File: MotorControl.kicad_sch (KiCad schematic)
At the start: 4 parts, among them U3 CSD18534Q5A, U4 CSD18534Q5A, U5 CSD18534Q5A

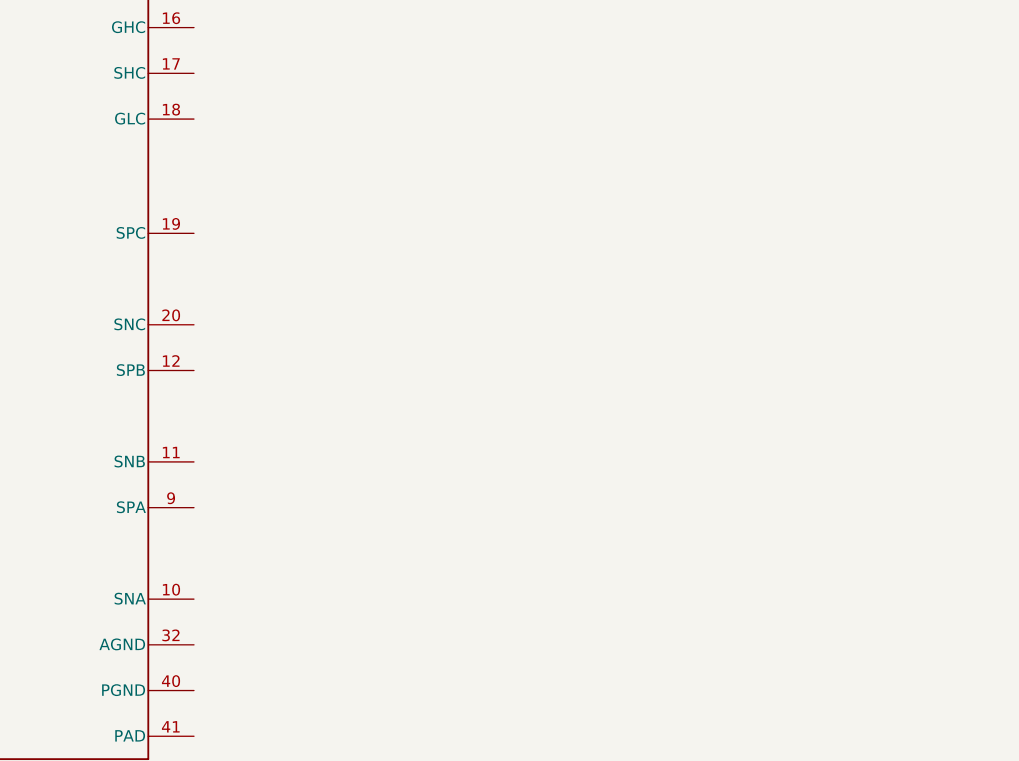
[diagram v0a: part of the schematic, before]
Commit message: wire sense resistors
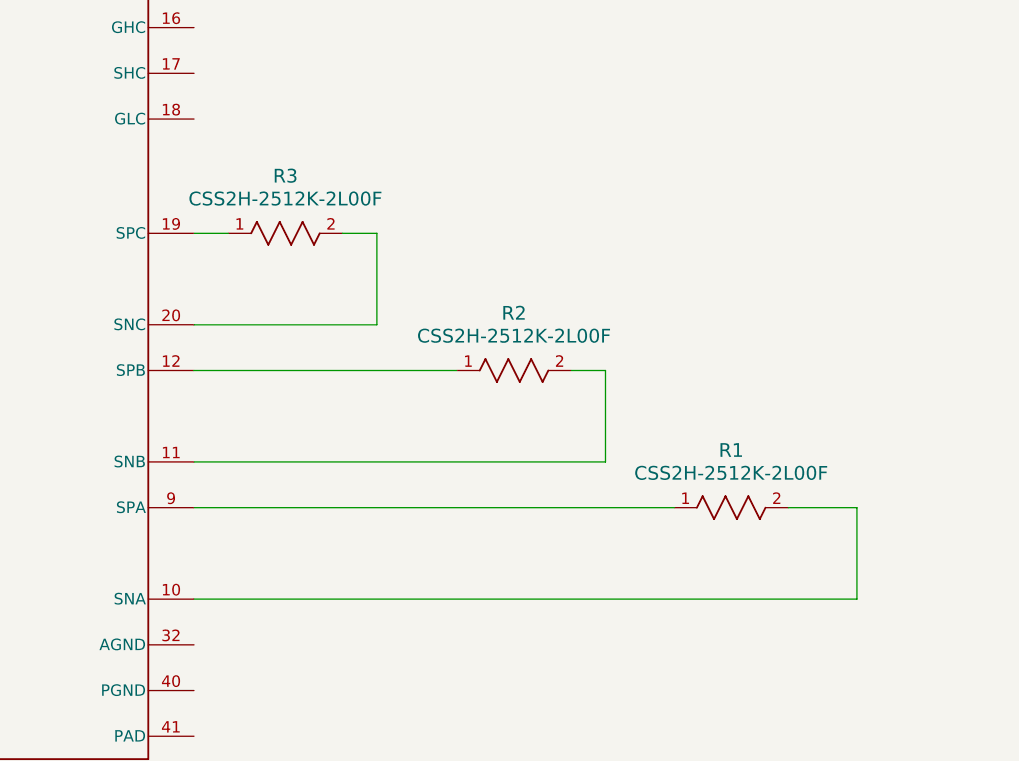
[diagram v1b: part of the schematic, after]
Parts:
- added R1, R2, R3: CSS2H-2512K-2L00F, RES_2L00x_BRN, symbol CSS2H_2512K_2L00F:CSS2H-2512K-2L00F
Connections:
- net at U?.10 (SNA): now also R1.2
- net at U?.11 (SNB): now also R2.2
- net at U?.12 (SPB): now also R2.1
- net at U?.19 (SPC): now also R3.1
- net at U?.20 (SNC): now also R3.2
- net at U?.9 (SPA): now also R1.1

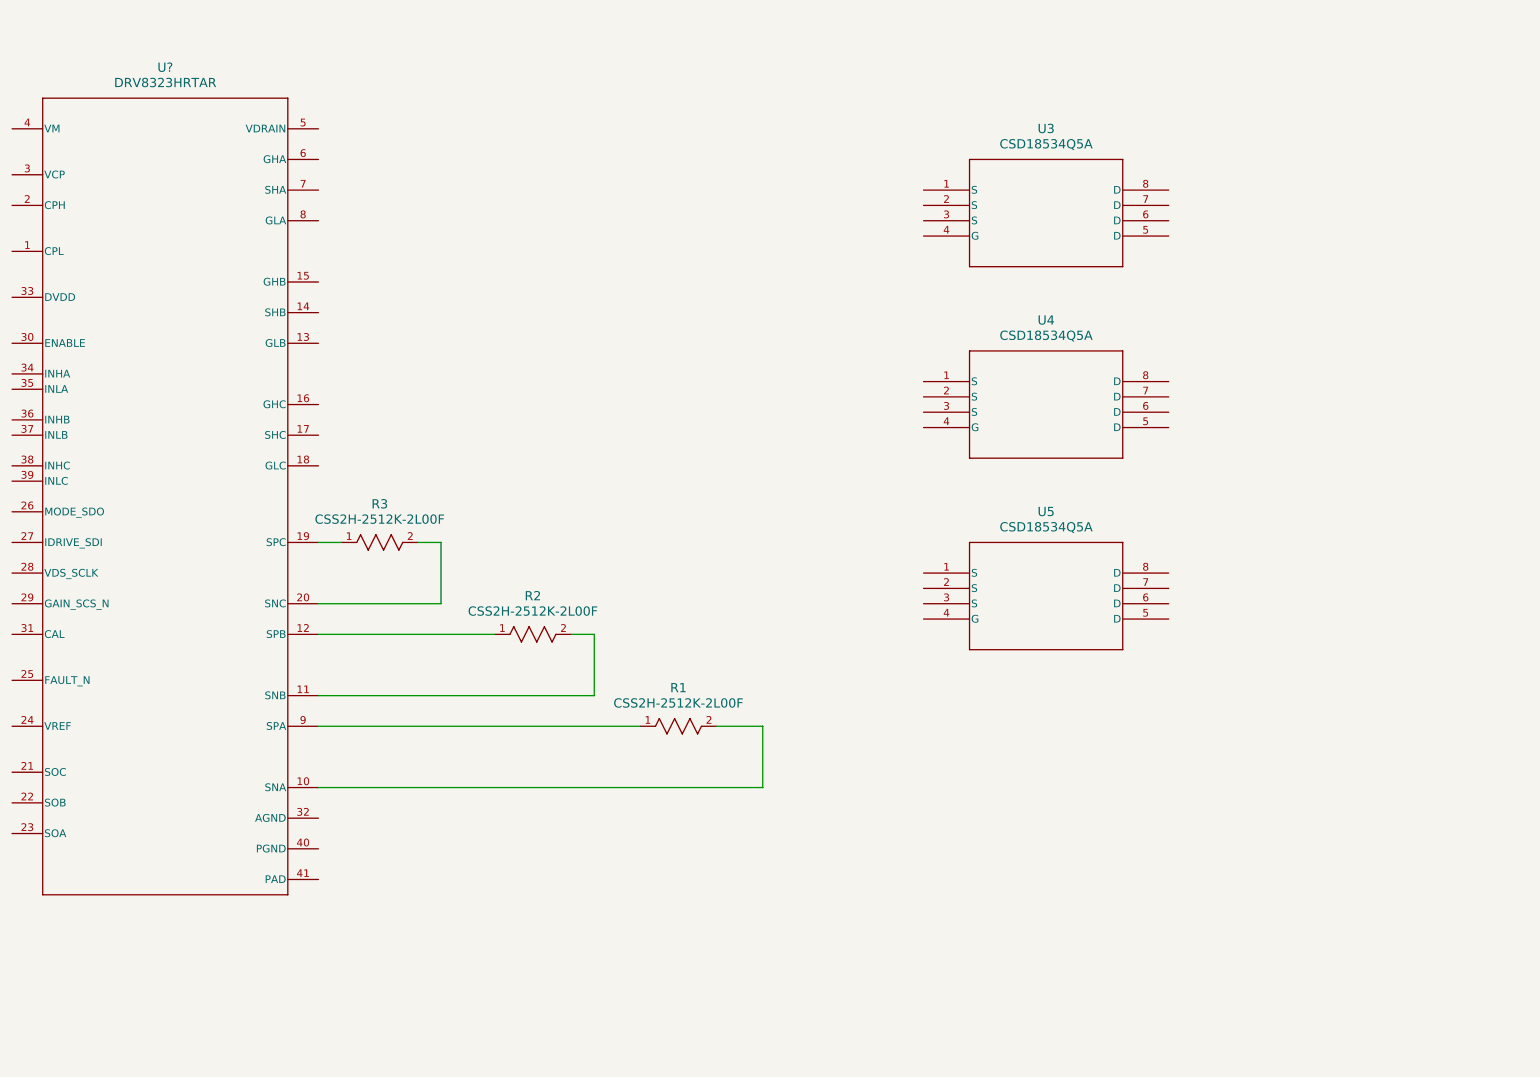
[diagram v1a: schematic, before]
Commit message: routed motor driver fets and shunts
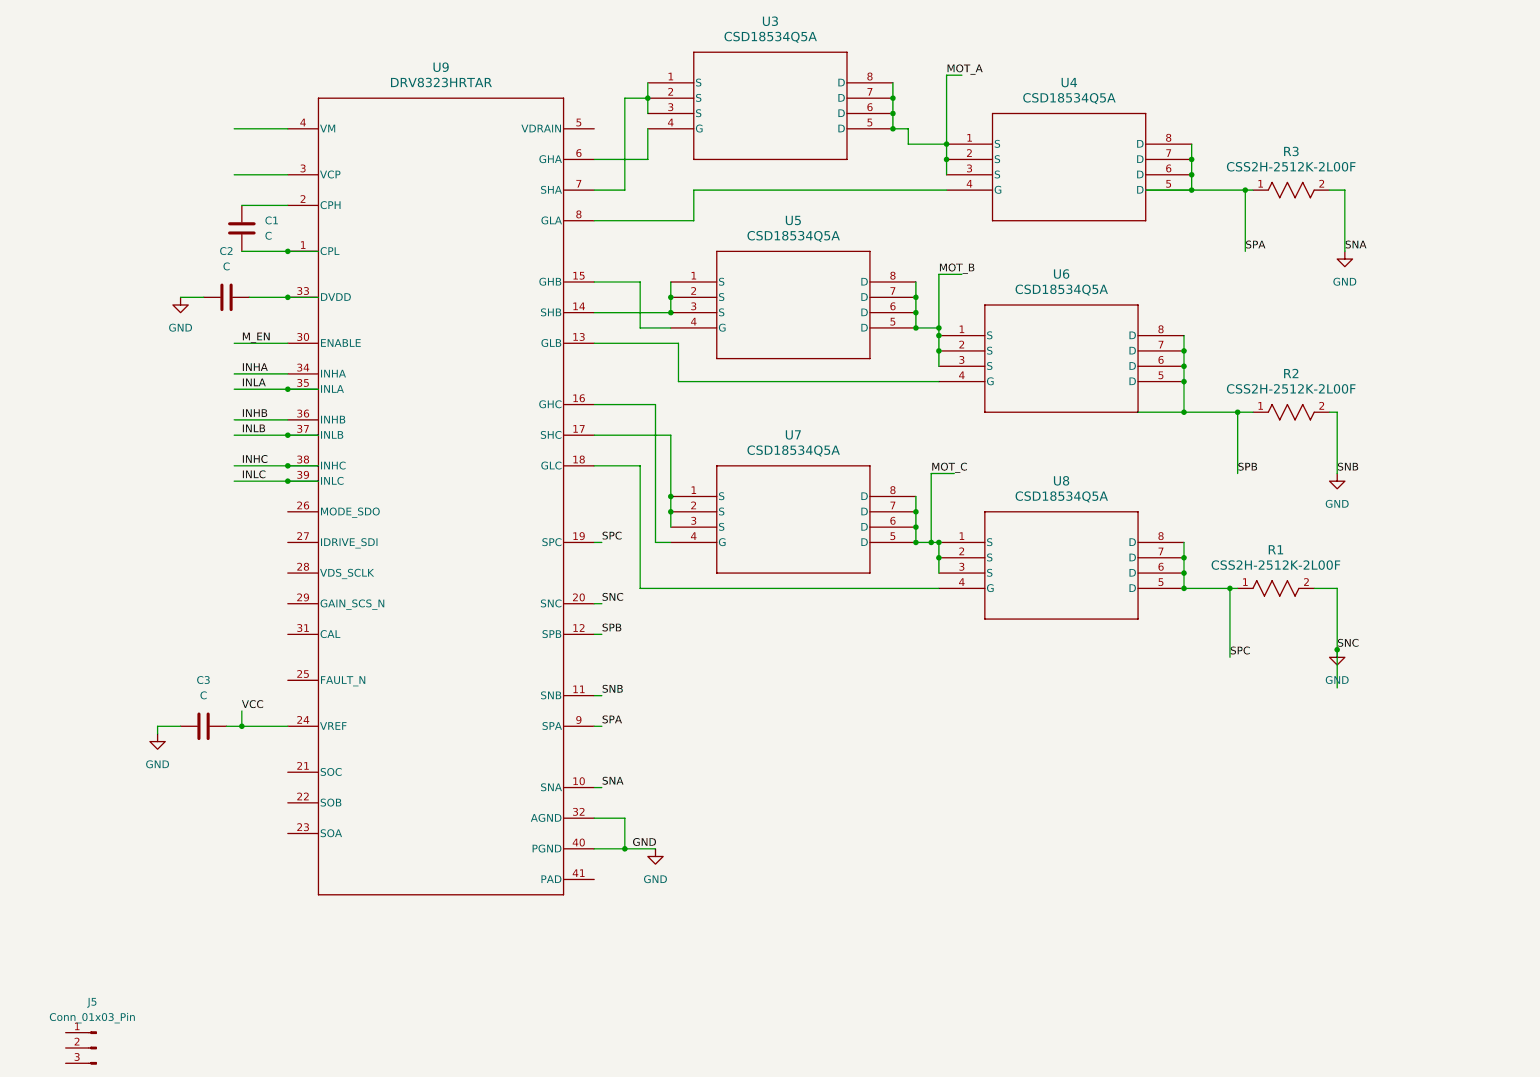
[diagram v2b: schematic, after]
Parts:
- added C1, C2, C3: C, symbol Device:C
- added J5: Conn_01x03_Pin, symbol Connector:Conn_01x03_Pin
- added U6, U7, U8: CSD18534Q5A, DQJ8, symbol CSD18534Q5A:CSD18534Q5A
- R1, R2, R3: footprint RES_2L00x_BRN -> Resistor_SMD:R_2512_6332Metric_Pad1.40x3.35mm_HandSolder
- gave numbers to parts that had none: 1
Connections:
- net SPA: now reaches U9.9 (SPA)
- net SPA: now also R3.1, U4.5 (D), U4.6 (D), U4.7 (D), U4.8 (D); no longer R1.1
- net GND: now reaches R1.2, U9.10 (SNA)
- net GND: now also R2.2, R3.2, U9.11 (SNB), U9.20 (SNC), U9.32 (AGND), U9.40 (PGND), C2.1, C3.1
- net at U5.1 (S): now also U5.2 (S), U5.3 (S), U9.14 (SHB)
- net at U5.4 (G): now also U9.15 (GHB)
- net MOT_B: now reaches U5.5 (D)
- net MOT_B: now also U5.6 (D), U5.7 (D), U5.8 (D), U6.1 (S), U6.2 (S), U6.3 (S)
- net at U9.1 (CPL): now also C1.2
- net SPB: now reaches R2.1, U9.12 (SPB)
- net SPB: now also U6.5 (D), U6.6 (D), U6.7 (D), U6.8 (D)
- net at U9.13 (GLB): now also U6.4 (G)
- net at U9.16 (GHC): now also U7.4 (G)
- net at U9.17 (SHC): now also U7.1 (S), U7.2 (S), U7.3 (S)
- net at U9.18 (GLC): now also U8.4 (G)
- net SPC: now reaches U9.19 (SPC)
- net SPC: now also R1.1, U8.5 (D), U8.6 (D), U8.7 (D), U8.8 (D); no longer R3.1
- net at U9.2 (CPH): now also C1.1
- net VCC: now reaches U9.24 (VREF)
- net VCC: now also C3.2
- net M_EN: now reaches U9.30 (ENABLE)
- net at U9.33 (DVDD): now also C2.2
- net INHA: now reaches U9.34 (INHA)
- net INLA: now reaches U9.35 (INLA)
- net INHB: now reaches U9.36 (INHB)
- net INLB: now reaches U9.37 (INLB)
- net INHC: now reaches U9.38 (INHC)
- net INLC: now reaches U9.39 (INLC)
- net at U9.6 (GHA): now also U3.4 (G)
- net at U9.7 (SHA): now also U3.1 (S), U3.2 (S), U3.3 (S)
- net at U9.8 (GLA): now also U4.4 (G)
- net MOT_A: now reaches U3.5 (D)
- net MOT_A: now also U3.6 (D), U3.7 (D), U3.8 (D), U4.1 (S), U4.2 (S), U4.3 (S)
- new net MOT_C: U7.5 (D), U7.6 (D), U7.7 (D), U7.8 (D), U8.1 (S), U8.2 (S), U8.3 (S)
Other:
- moved on the sheet: R1, R2, R3, U3, U4, U5, U9

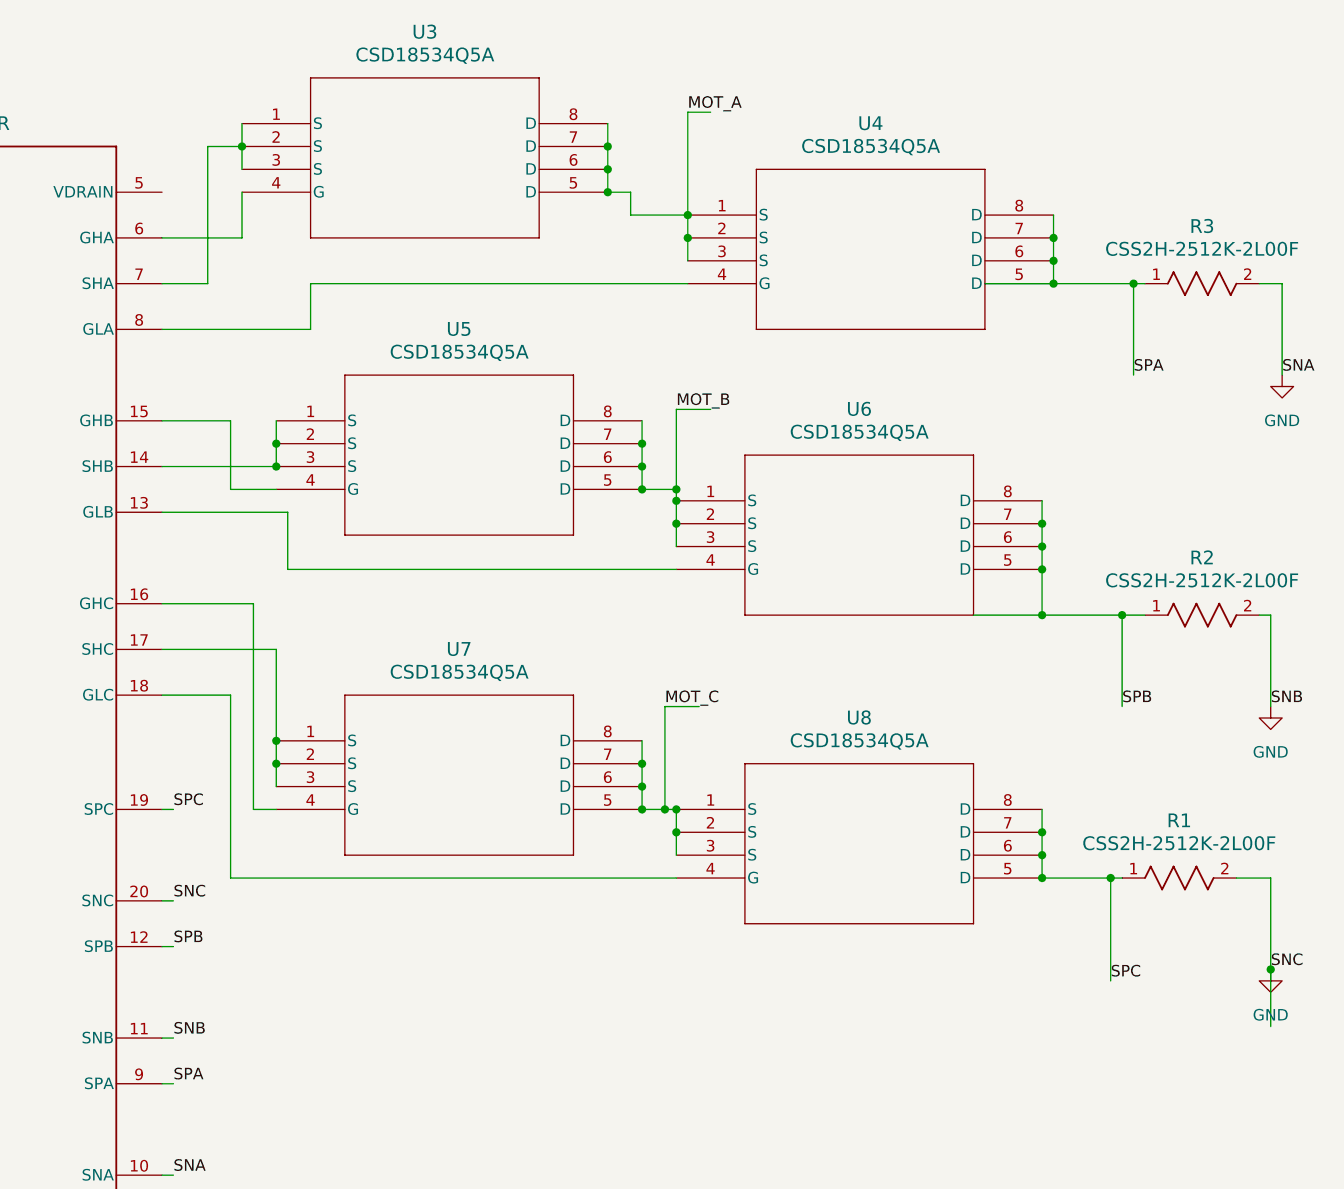
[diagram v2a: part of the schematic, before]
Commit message: route all 3 fets with shunts in a vertical line
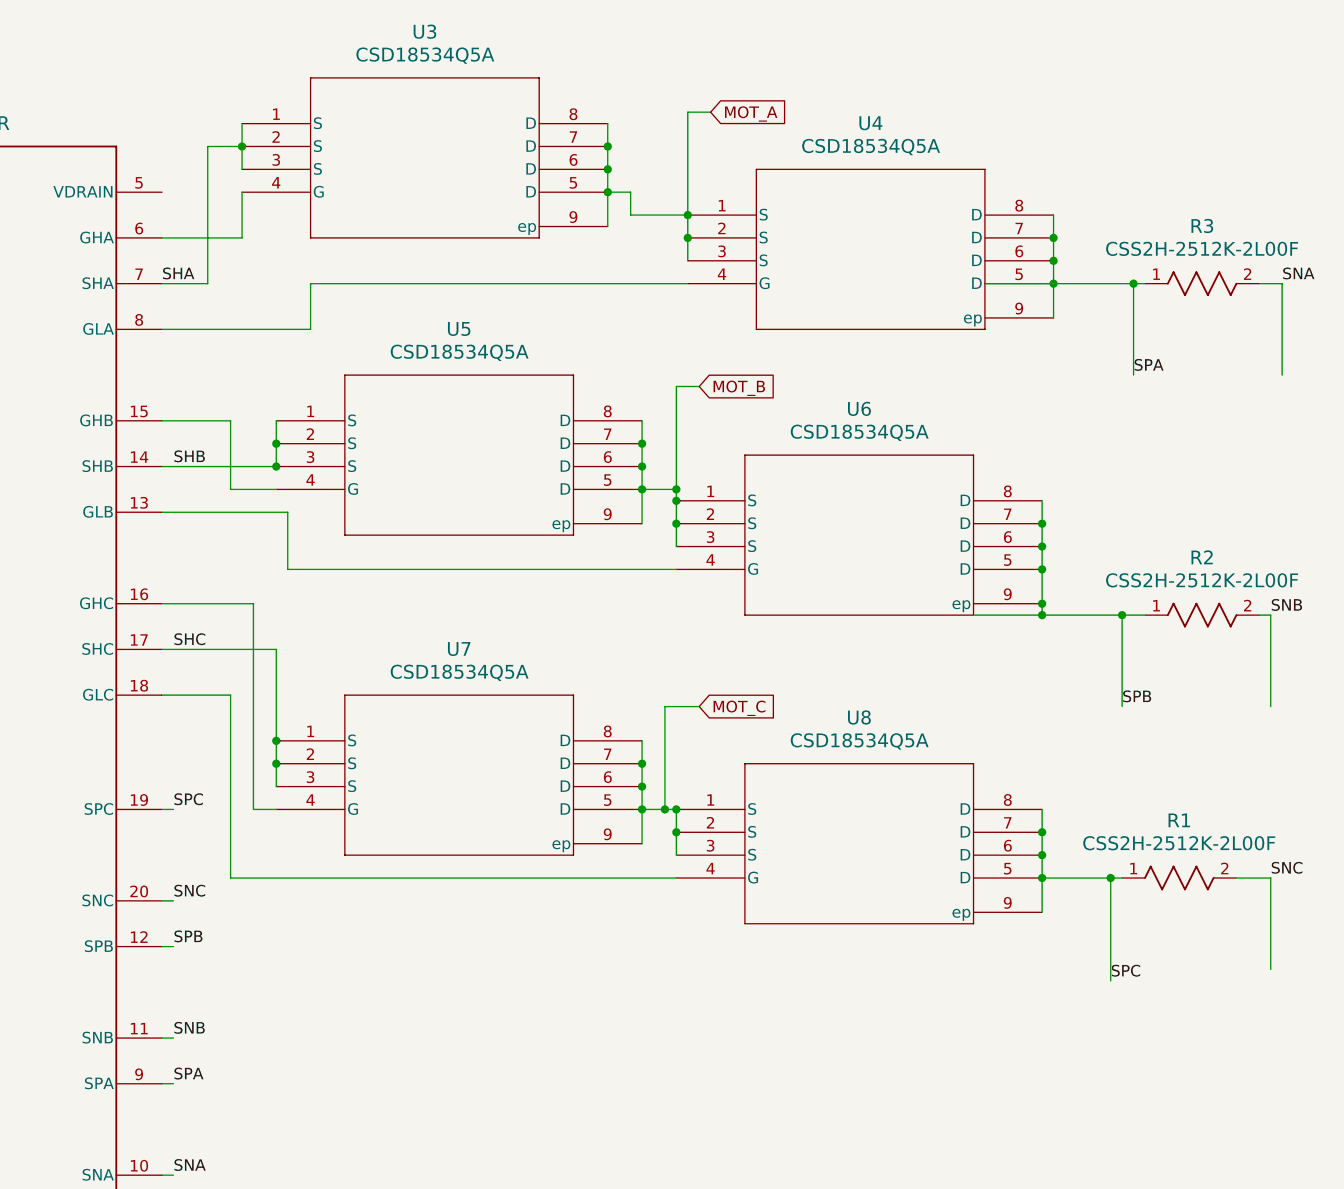
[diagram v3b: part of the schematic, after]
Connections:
- net GND: no longer R1.2, R2.2, R3.2, U9.10 (SNA), U9.11 (SNB), U9.20 (SNC)
- net MOT_A: now also U3.9 (ep)
- net MOT_B: now also U5.9 (ep)
- net MOT_C: now also U7.9 (ep)
- net SPA: now also U4.9 (ep)
- net SPB: now also U6.9 (ep)
- net SPC: now also U8.9 (ep)
- net SHB: now reaches U5.1 (S), U5.2 (S), U5.3 (S), U9.14 (SHB)
- net SHC: now reaches U7.1 (S), U7.2 (S), U7.3 (S), U9.17 (SHC)
- net SHA: now reaches U3.1 (S), U3.2 (S), U3.3 (S), U9.7 (SHA)
- new net SNA: R3.2, U9.10 (SNA)
- new net SNB: R2.2, U9.11 (SNB)
- new net SNC: R1.2, U9.20 (SNC)
